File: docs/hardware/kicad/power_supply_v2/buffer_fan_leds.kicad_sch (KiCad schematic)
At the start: 11 parts, among them M1 Fan_4pin, U19 SN74AHCT125N

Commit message: updated schematic for LC filters and added voltage injection to other bucks
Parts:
- renumbered C42 to C43, R26 to R28, R27 to R29, R28 to R30, R29 to R31
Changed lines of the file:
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@@
-	)
-	(junction
-		(at 62.23 40.64)
-		(diameter 0)
-		(color 0 0 0 0)
 	)
 	(junction
@@
 	(wire
 		(pts
-			(xy 52.07 40.64) (xy 62.23 40.64)
+			(xy 52.07 40.64) (xy 72.39 40.64)
 		)
 		(stroke
@@
 		(pts
 			(xy 59.69 87.63) (xy 62.23 87.63)
-		)
-		(stroke
-			(width 0)
-			(type default)
-		)
-	)
-	(wire
-		(pts
-			(xy 62.23 40.64) (xy 72.39 40.64)
 		)
 		(stroke
@@
 		(on_board yes)
 		(dnp no)
-		(property "Reference" "C42"
+		(property "Reference" "C43"
 			(at 73.66 45.212 90)
 			(effects
@@
 			(project "power_supply_v2"
 				(path "/cac0009d-9d0b-438f-a386-67368a9db47f/f46472e6-7163-47dd-a53b-dd0b116ef3da"
-					(reference "C42")
+					(reference "C43")
 					(unit 1)
 				)
@@
 		(dnp no)
 		(fields_autoplaced yes)
-		(property "Reference" "R27"
+		(property "Reference" "R29"
 			(at 52.07 93.9799 0)
 			(effects
@@
 			(project "power_supply_v2"
 				(path "/cac0009d-9d0b-438f-a386-67368a9db47f/f46472e6-7163-47dd-a53b-dd0b116ef3da"
-					(reference "R27")
+					(reference "R29")
 					(unit 1)
 				)
@@
 		(dnp no)
 		(fields_autoplaced yes)
-		(property "Reference" "R28"
+		(property "Reference" "R30"
 			(at 88.9 44.45 90)
 			(effects
@@
 			(project "power_supply_v2"
 				(path "/cac0009d-9d0b-438f-a386-67368a9db47f/f46472e6-7163-47dd-a53b-dd0b116ef3da"
-					(reference "R28")
+					(reference "R30")
 					(unit 1)
 				)
@@
 	)
 	(symbol
-		(lib_id "power:PWR_FLAG")
-		(at 62.23 40.64 0)
-		(unit 1)
-		(exclude_from_sim no)
-		(in_bom yes)
-		(on_board yes)
-		(dnp no)
-		(fields_autoplaced yes)
-		(property "Reference" "#FLG01"
-			(at 62.23 38.735 0)
-			(effects
-				(font
-					(size 1.27 1.27)
-				)
-				(hide yes)
-			)
-		)
-		(property "Value" "PWR_FLAG"
-			(at 62.23 35.56 0)
-			(effects
-				(font
-					(size 1.27 1.27)
-				)
-			)
-		)
-		(property "Footprint" ""
-			(at 62.23 40.64 0)
-			(effects
-				(font
-					(size 1.27 1.27)
-				)
-				(hide yes)
-			)
-		)
-		(property "Datasheet" "~"
-			(at 62.23 40.64 0)
-			(effects
-				(font
-					(size 1.27 1.27)
-				)
-				(hide yes)
-			)
-		)
-		(property "Description" "Special symbol for telling ERC where power comes from"
-			(at 62.23 40.64 0)
-			(effects
-				(font
-					(size 1.27 1.27)
-				)
-				(hide yes)
-			)
-		)
-		(pin "1"
-		)
-		(instances
-			(project "power_supply_v2"
-				(path "/cac0009d-9d0b-438f-a386-67368a9db47f/f46472e6-7163-47dd-a53b-dd0b116ef3da"
-					(reference "#FLG01")
-					(unit 1)
-				)
-			)
-		)
-	)
-	(symbol
 		(lib_id "power:+3.3VA")
 		(at 119.38 69.85 0)
@@
 		(dnp no)
 		(fields_autoplaced yes)
-		(property "Reference" "R26"
+		(property "Reference" "R28"
 			(at 41.91 93.9799 0)
 			(effects
@@
 			(project "power_supply_v2"
 				(path "/cac0009d-9d0b-438f-a386-67368a9db47f/f46472e6-7163-47dd-a53b-dd0b116ef3da"
-					(reference "R26")
+					(reference "R28")
 					(unit 1)
 				)
@@
 		(dnp no)
 		(fields_autoplaced yes)
-		(property "Reference" "R29"
+		(property "Reference" "R31"
 			(at 111.76 72.3899 0)
 			(effects
@@
 			(project "power_supply_v2"
 				(path "/cac0009d-9d0b-438f-a386-67368a9db47f/f46472e6-7163-47dd-a53b-dd0b116ef3da"
-					(reference "R29")
+					(reference "R31")
 					(unit 1)
 				)

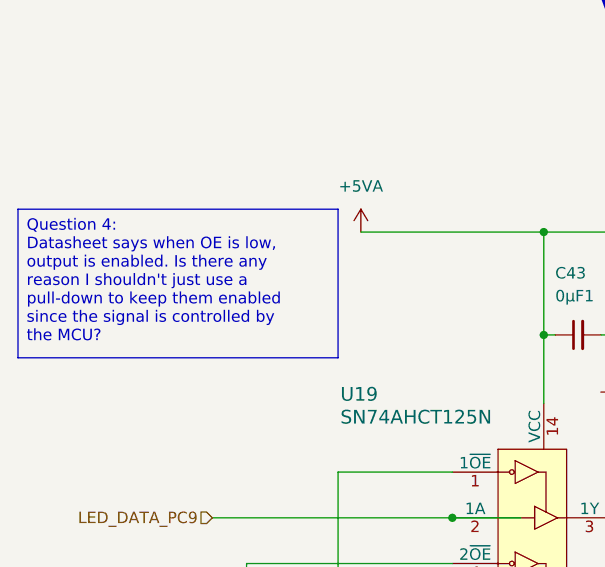
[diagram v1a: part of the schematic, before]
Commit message: rework buck resistor divider values + add fb injection to 3V3 and 5V rail bucks
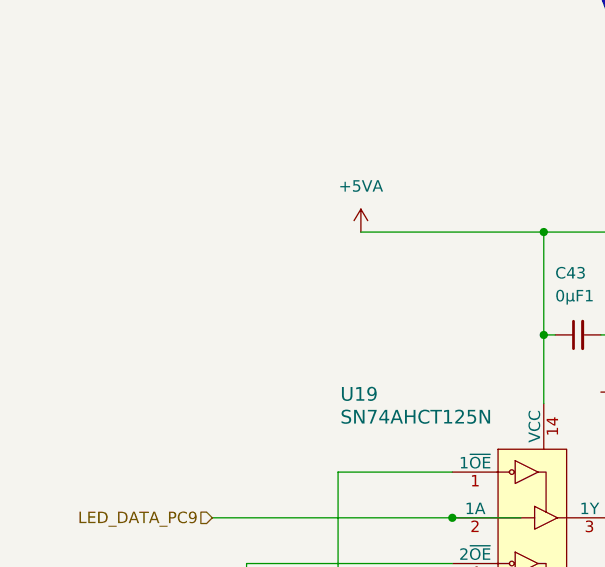
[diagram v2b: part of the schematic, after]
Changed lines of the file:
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@@
 	(title_block
 		(title "Digital Variable DC Bench Power Supply")
-		(date "2026-04-27")
-		(rev "1")
+		(date "2026-04-30")
+		(rev "A2")
 	)
 	(text "VOLTAGE BUFFER + FAN & LEDs"
@@
 		)
 	)
-	(text_box "Question 4:\nDatasheet says when OE is low, output is enabled. Is there any reason I shouldn't just use a pull-down to keep them enabled since the signal is controlled by the MCU?"
-		(exclude_from_sim no)
-		(at 13.97 38.1 0)
-		(size 35.56 16.51)
-		(margins 0.9525 0.9525 0.9525 0.9525)
-		(stroke
-			(width 0)
-			(type solid)
-		)
-		(fill
-			(type none)
-		)
-		(effects
-			(font
-				(size 1.27 1.27)
-			)
-			(justify left top)
-		)
-	)

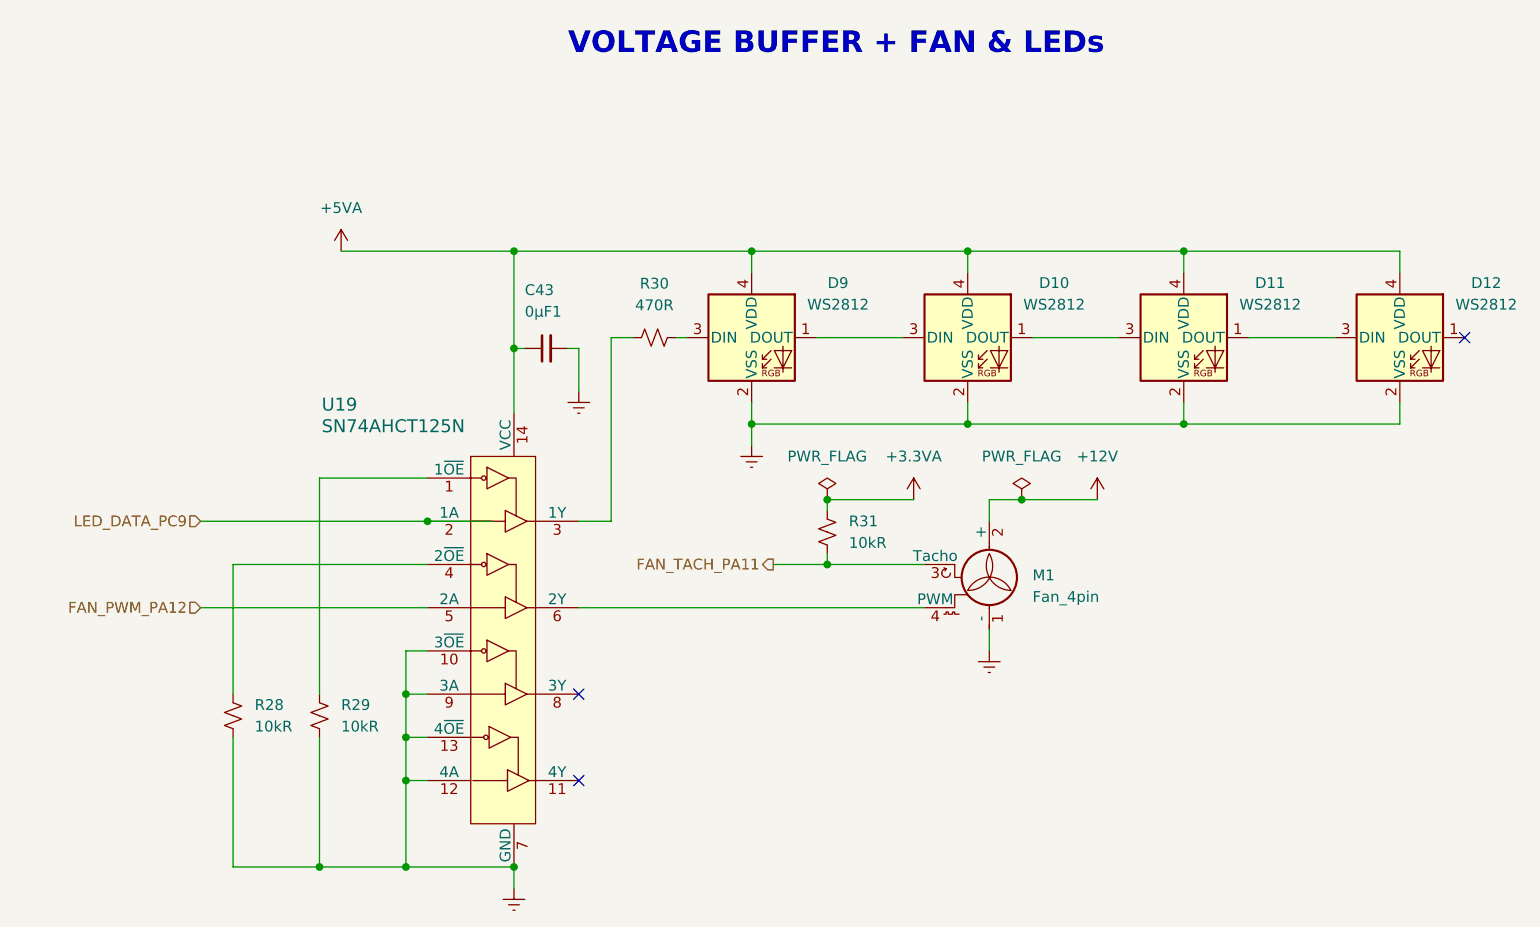
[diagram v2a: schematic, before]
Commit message: remove redundant switches for variable rail
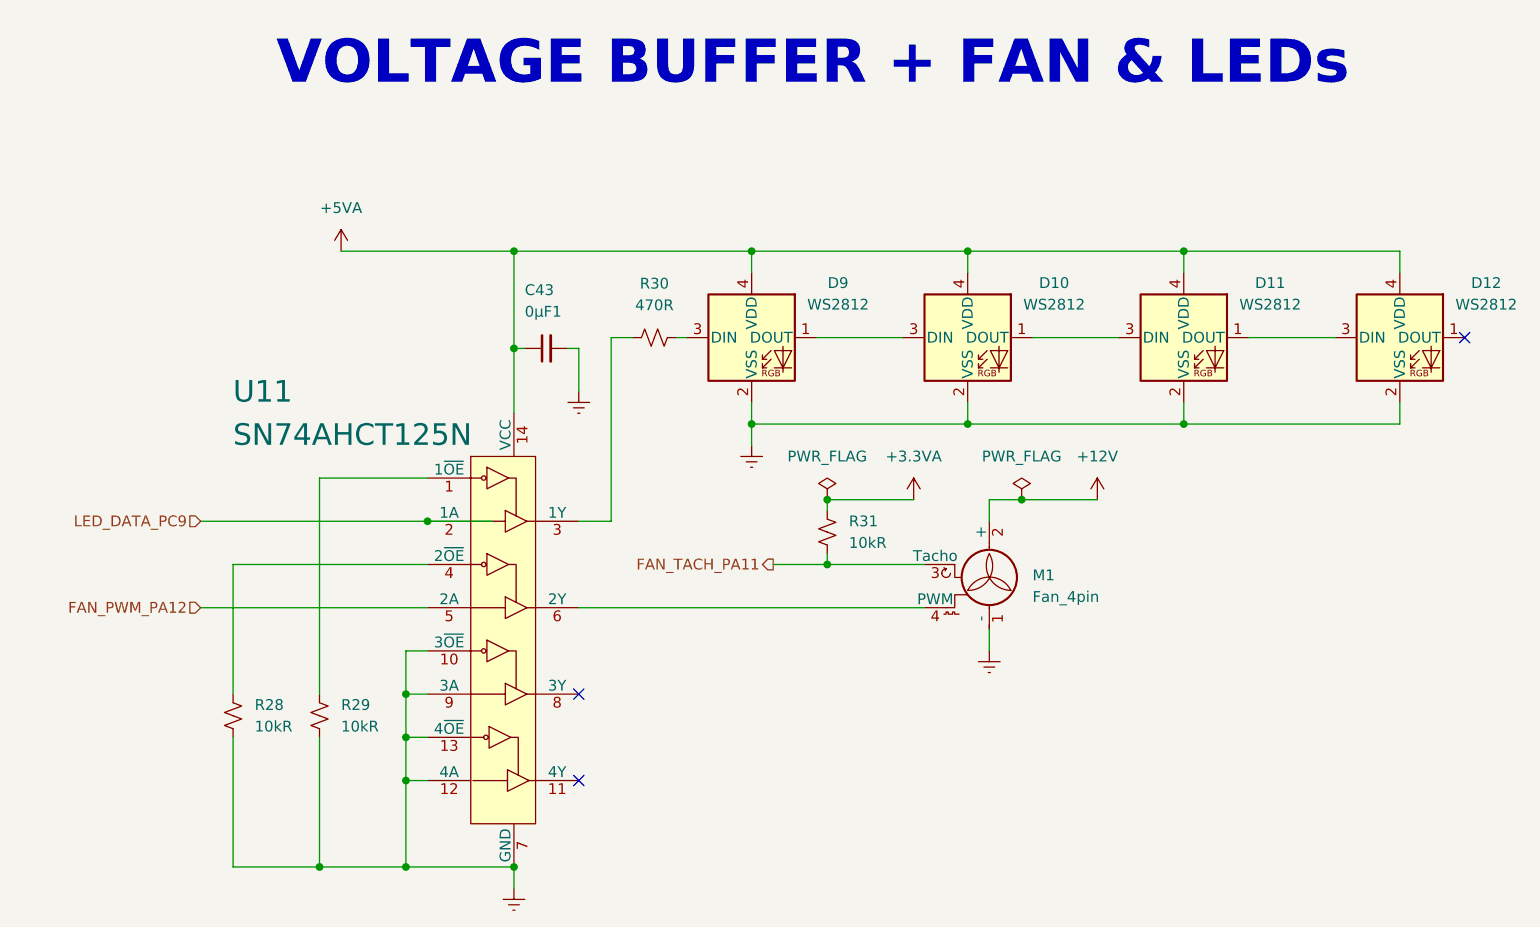
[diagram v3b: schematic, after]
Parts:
- renumbered U19 to U11
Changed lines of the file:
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@@
 	(title_block
 		(title "Digital Variable DC Bench Power Supply")
-		(date "2026-04-30")
-		(rev "A2")
+		(date "2026-05-01")
+		(rev "A3")
 	)
 	(text "VOLTAGE BUFFER + FAN & LEDs"
 		(exclude_from_sim no)
-		(at 78.74 17.78 0)
+		(at 44.45 21.59 0)
 		(effects
 			(font
-				(size 2.54 2.54)
+				(size 5.08 5.08)
 				(thickness 1.016)
 				(bold yes)
@@
 		(on_board yes)
 		(dnp no)
-		(property "Reference" "U19"
-			(at 49.784 58.674 0)
-			(effects
-				(font
-					(size 1.524 1.524)
+		(property "Reference" "U11"
+			(at 39.37 57.15 0)
+			(effects
+				(font
+					(size 2.54 2.54)
 				)
 				(justify left)
@@
 		)
 		(property "Value" "SN74AHCT125N"
-			(at 49.784 61.214 0)
-			(effects
-				(font
-					(size 1.524 1.524)
+			(at 39.37 62.23 0)
+			(effects
+				(font
+					(size 2.54 2.54)
 				)
 				(justify left)
@@
 			(project "power_supply_v2"
 				(path "/cac0009d-9d0b-438f-a386-67368a9db47f/f46472e6-7163-47dd-a53b-dd0b116ef3da"
-					(reference "U19")
+					(reference "U11")
 					(unit 1)
 				)
